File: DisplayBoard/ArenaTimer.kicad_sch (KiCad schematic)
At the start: 52 parts, among them J1 Blue ready-up, J10 Red ready-up, J11 SPARE_IO, J12 Screw_Terminal_01x03, J13 WAGO, J14 WAGO, J15 Conn_01x15_Socket, J16 Conn_01x15_Socket, J17 SPARE IO, J18 SPARE 3.3V, J19 SPARE 5V, J2 Conn_01x02_Socket, J20 SPARE GND, J21 SPARE GND, J3 Conn_01x02_Pin, J4 GND, J5 5V, J6 GND, J7 5V, J8 PJ-082BH, J9 Conn_01x06_Pin, K1 G5V-2_Split, Q1 BSS138, Q2 BSS138

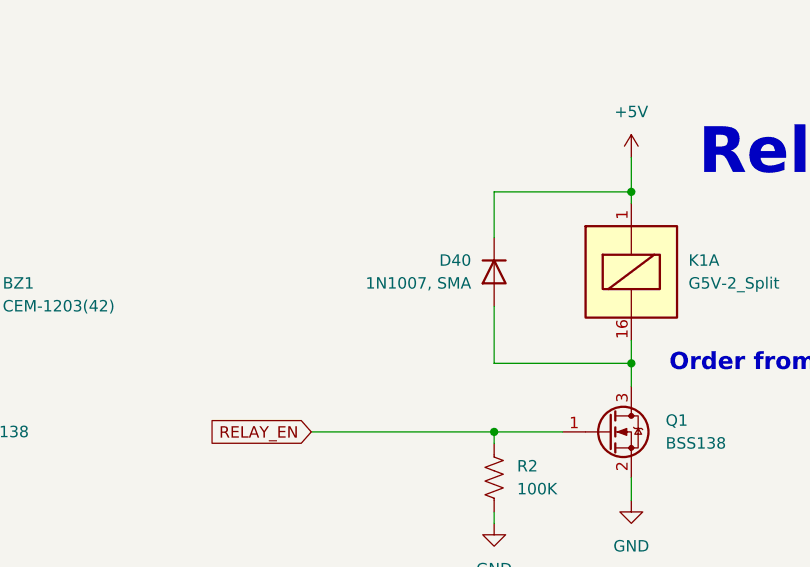
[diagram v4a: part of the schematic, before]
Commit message: fix diode MPN
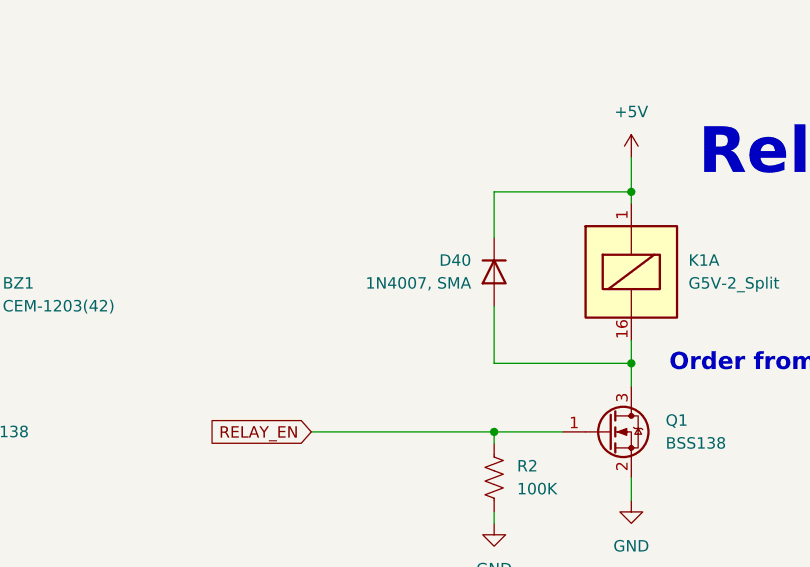
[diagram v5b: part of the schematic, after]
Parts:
- D40: value 1N1007, SMA -> 1N4007, SMA
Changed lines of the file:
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@@
 			)
 		)
-		(property "Value" "1N1007, SMA"
+		(property "Value" "1N4007, SMA"
 			(at 308.61 198.1199 90)
 			(show_name no)

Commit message: update LCSC PN for fets to match sc-70 footprint on board
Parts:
- Q1, Q2: LCSC C5224267 -> C5224279
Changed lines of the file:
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@@
 			)
 		)
-		(property "LCSC" "C5224267"
+		(property "LCSC" "C5224279"
 			(at 323.85 214.63 0)
 			(hide yes)
@@
 			)
 		)
-		(property "LCSC" "C5224267"
+		(property "LCSC" "C5224279"
 			(at 246.38 213.36 0)
 			(hide yes)
